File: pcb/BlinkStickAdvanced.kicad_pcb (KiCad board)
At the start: 2 copper layers, 37.1 x 59.3 mm, 31 parts, among them J1 POWER, J2 USB_B_Micro, J3 ADD_HEADER_B, J4 ADD_HEADER_G, J5 ADD_HEADER_R, J6 RGB_HEADER, J7 RGB_HEADER, Q1 IRLR8726, Q2 IRLR8726, Q3 IRLR8726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

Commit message: PCB Change Silkscreen
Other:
- board text added: "BlinkStick Advanced (c) Foxdogface & Agile Inovative Ltd github.com/Foxdogface/BlinkStickAdvanced"
- board text removed: "BlinkStick Advanced Foxdogface & Agile Inovative Ltd"
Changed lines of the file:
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@@
   (gr_poly
     (pts
-      (xy 49.852241 42.689652)
-      (xy 49.852241 43.138906)
-      (xy 45.093779 43.138906)
-      (xy 45.093779 44.037292)
-      (xy 49.852241 44.037292)
-      (xy 49.852241 44.48691)
-      (xy 55.64193 44.48691)
-      (xy 55.64193 42.689652)
-      (xy 49.852241 42.689652)
-    ) (layer "B.SilkS") (width 0.2) (fill solid))
+      (xy 55.181249 76.88263)
+      (xy 55.181249 76.972481)
+      (xy 54.229556 76.972481)
+      (xy 54.229556 77.152158)
+      (xy 55.181249 77.152158)
+      (xy 55.181249 77.242082)
+      (xy 56.339186 77.242082)
+      (xy 56.339186 76.88263)
+      (xy 55.181249 76.88263)
+    ) (layer "B.SilkS") (width 0.008) (fill solid))
   (gr_poly
     (pts
-      (xy 49.852241 49.926867)
-      (xy 49.852241 50.376667)
-      (xy 43.596186 50.376667)
-      (xy 43.596186 51.27487)
-      (xy 49.852241 51.27487)
-      (xy 49.852241 51.724306)
-      (xy 55.64193 51.724306)
-      (xy 55.64193 49.926867)
-      (xy 49.852241 49.926867)
-    ) (layer "B.SilkS") (width 0.2) (fill solid))
+      (xy 55.181249 78.330073)
+      (xy 55.181249 78.420033)
+      (xy 53.930038 78.420033)
+      (xy 53.930038 78.599674)
+      (xy 55.181249 78.599674)
+      (xy 55.181249 78.689561)
+      (xy 56.339186 78.689561)
+      (xy 56.339186 78.330073)
+      (xy 55.181249 78.330073)
+    ) (layer "B.SilkS") (width 0.008) (fill solid))
   (gr_poly
     (pts
-      (xy 61.13256 53.3883)
-      (xy 61.13256 41.142235)
-      (xy 64.593265 41.142235)
-      (xy 64.908331 41.150203)
-      (xy 65.21926 41.173849)
-      (xy 65.525669 41.212789)
-      (xy 65.827172 41.266638)
-      (xy 66.123385 41.335011)
-      (xy 66.413924 41.417524)
-      (xy 66.698403 41.513792)
-      (xy 66.976437 41.62343)
-      (xy 67.247643 41.746054)
-      (xy 67.511635 41.881279)
-      (xy 67.768029 42.02872)
-      (xy 68.01644 42.187992)
-      (xy 68.256483 42.358711)
-      (xy 68.487774 42.540491)
-      (xy 68.709928 42.732949)
-      (xy 68.922561 42.9357)
-      (xy 69.125286 43.148359)
-      (xy 69.317721 43.37054)
-      (xy 69.49948 43.60186)
-      (xy 69.670178 43.841934)
-      (xy 69.829432 44.090376)
-      (xy 69.976855 44.346803)
-      (xy 70.112064 44.61083)
-      (xy 70.234673 44.882071)
-      (xy 70.344299 45.160143)
-      (xy 70.440556 45.444659)
-      (xy 70.52306 45.735237)
-      (xy 70.591425 46.03149)
-      (xy 70.645268 46.333035)
-      (xy 70.684204 46.639487)
-      (xy 70.707847 46.95046)
-      (xy 70.715814 47.26557)
-      (xy 70.707846 47.580594)
-      (xy 70.6842 47.891488)
-      (xy 70.645259 48.197868)
-      (xy 70.59141 48.499348)
-      (xy 70.523037 48.795544)
-      (xy 70.440524 49.086071)
-      (xy 70.344257 49.370543)
-      (xy 70.234621 49.648575)
-      (xy 70.112 49.919783)
-      (xy 69.97678 50.183782)
-      (xy 69.829345 50.440185)
-      (xy 69.670079 50.688609)
-      (xy 69.499369 50.928668)
-      (xy 69.317599 51.159977)
-      (xy 69.125153 51.382151)
-      (xy 68.922417 51.594805)
-      (xy 68.709775 51.797554)
-      (xy 68.487613 51.990013)
-      (xy 68.256315 52.171798)
-      (xy 68.016266 52.342521)
-      (xy 67.767851 52.5018)
-      (xy 67.511455 52.649249)
-      (xy 67.247462 52.784482)
-      (xy 66.976258 52.907115)
-      (xy 66.698228 53.016762)
-      (xy 66.413757 53.11304)
-      (xy 66.123228 53.195561)
-      (xy 65.827028 53.263943)
-      (xy 65.52554 53.317798)
-      (xy 65.219151 53.356743)
-      (xy 64.908244 53.380393)
-      (xy 64.593205 53.388361)
-      (xy 61.13256 53.388361)
-      (xy 61.13256 53.3883)
-    ) (layer "B.SilkS") (width 0.2) (fill solid))
+      (xy 57.250936 76.320222)
+      (xy 56.532166 76.320222)
+      (xy 56.532166 79.381775)
+      (xy 57.250936 79.381775)
+      (xy 57.250936 76.320222)
+    ) (layer "B.SilkS") (width 0.008) (fill solid))
   (gr_poly
     (pts
-      (xy 60.200676 39.877612)
-      (xy 56.606829 39.877612)
-      (xy 56.606829 55.185377)
-      (xy 60.200677 55.185377)
-      (xy 60.200677 39.877612)
-      (xy 60.200676 39.877612)
-    ) (layer "B.SilkS") (width 0.2) (fill solid))
+      (xy 57.437312 79.02236)
+      (xy 57.437312 76.573147)
+      (xy 58.129453 76.573147)
+      (xy 58.192467 76.57474)
+      (xy 58.254652 76.579469)
+      (xy 58.315934 76.587257)
+      (xy 58.376235 76.598027)
+      (xy 58.435477 76.611702)
+      (xy 58.493585 76.628204)
+      (xy 58.550481 76.647458)
+      (xy 58.606088 76.669386)
+      (xy 58.660329 76.69391)
+      (xy 58.713127 76.720955)
+      (xy 58.764406 76.750444)
+      (xy 58.814088 76.782298)
+      (xy 58.862097 76.816442)
+      (xy 58.908355 76.852798)
+      (xy 58.952786 76.891289)
+      (xy 58.995313 76.93184)
+      (xy 59.035858 76.974371)
+      (xy 59.074345 77.018808)
+      (xy 59.110696 77.065072)
+      (xy 59.144836 77.113086)
+      (xy 59.176687 77.162775)
+      (xy 59.206171 77.21406)
+      (xy 59.233213 77.266866)
+      (xy 59.257735 77.321114)
+      (xy 59.27966 77.376728)
+      (xy 59.298912 77.433631)
+      (xy 59.315412 77.491747)
+      (xy 59.329085 77.550998)
+      (xy 59.339854 77.611307)
+      (xy 59.347641 77.672597)
+      (xy 59.35237 77.734792)
+      (xy 59.353963 77.797814)
+      (xy 59.35237 77.860818)
+      (xy 59.34764 77.922997)
+      (xy 59.339852 77.984273)
+      (xy 59.329082 78.044569)
+      (xy 59.315408 78.103808)
+      (xy 59.298905 78.161914)
+      (xy 59.279652 78.218808)
+      (xy 59.257725 78.274415)
+      (xy 59.2332 78.328656)
+      (xy 59.206156 78.381456)
+      (xy 59.176669 78.432737)
+      (xy 59.144816 78.482421)
+      (xy 59.110674 78.530433)
+      (xy 59.07432 78.576695)
+      (xy 59.035831 78.62113)
+      (xy 58.995284 78.663661)
+      (xy 58.952755 78.70421)
+      (xy 58.908323 78.742702)
+      (xy 58.862063 78.779059)
+      (xy 58.814054 78.813204)
+      (xy 58.764371 78.84506)
+      (xy 58.713091 78.874549)
+      (xy 58.660293 78.901596)
+      (xy 58.606052 78.926123)
+      (xy 58.550446 78.948052)
+      (xy 58.493552 78.967308)
+      (xy 58.435446 78.983812)
+      (xy 58.376206 78.997488)
+      (xy 58.315908 79.008259)
+      (xy 58.254631 79.016048)
+      (xy 58.192449 79.020778)
+      (xy 58.129441 79.022372)
+      (xy 57.437312 79.022372)
+      (xy 57.437312 79.02236)
+    ) (layer "B.SilkS") (width 0.008) (fill solid))
   (gr_line (start 70.618 57.604) (end 70.618 56.334) (layer "F.SilkS") (width 0.12))
   (gr_line (start 70.618 70.7485) (end 70.618 69.4785) (layer "F.SilkS") (width 0.12))
@@
   (gr_arc (start 41.154 93.435) (mid 39.357949 92.691051) (end 38.614 90.895) (layer "Edge.Cuts") (width 0.1))
   (gr_line (start 73.158 93.442349) (end 41.154 93.435) (layer "Edge.Cuts") (width 0.1))
-  (gr_text "BlinkStick Advanced\nFoxdogface & Agile Inovative Ltd" (at 46.736 68.326 270) (layer "B.SilkS")
-    (effects (font (size 1 1) (thickness 0.15)) (justify mirror))
+  (gr_text "BlinkStick Advanced\n(c) Foxdogface & Agile Inovative Ltd\ngithub.com/Foxdogface/BlinkStickAdvanced" (at 56.642 75.819 270) (layer "B.SilkS")
+    (effects (font (size 1 1) (thickness 0.15)) (justify left mirror))
   )
   (gr_text "+12" (at 69.602 69.4785 90) (layer "F.SilkS")
@@
     (effects (font (size 1 1) (thickness 0.15)))
   )
-  (gr_text "BlinkStick Advanced\nRev 1.0\n" (at 63.881 74.549 90) (layer "F.SilkS")
+  (gr_text "BlinkStick Advanced\nRev 1.0\n" (at 63.5 78.74 90) (layer "F.SilkS")
     (effects (font (size 1 1) (thickness 0.15)) (justify left))
   )
@@
     (effects (font (size 0.8 0.8) (thickness 0.12)))
   )
-  (gr_text "DI" (at 44.71 74.294 270) (layer "F.SilkS")
+  (gr_text "DI" (at 44.71 74.294) (layer "F.SilkS")
     (effects (font (size 1 1) (thickness 0.15)))
   )
@@
     )
   )
+  (group "" (id b1dad93c-ba77-40bd-9b75-65e2d6f9b5a1)
+    (members
+      4ccb0e93-36f7-4d7b-baba-2457a90267b7
+      5e182438-6e6f-45ba-bef5-6be708805673
+      5ed8deae-e8d8-451d-b355-245f684ec0f6
+      9fa8af66-62ad-41ac-afee-78344131d7e2
+    )
+  )
   (group "" (id dc577978-f61c-428e-9244-b42fcfc07f25)
     (members
@@
     )
   )
-  (group "" (id e15cedca-0c1c-4c6b-b473-17ab02d76cf9)
-    (members
-      057dff60-5b63-4365-8092-fe40ca4f6ba6
-      94f916ed-7d8d-4c18-a00c-ed22517e241d
-      f2962283-8d92-4dc3-8a08-f6b3cc18df8b
-      f6cc9d27-2a76-4bc5-bcfe-60cd92efc84c
-    )
-  )

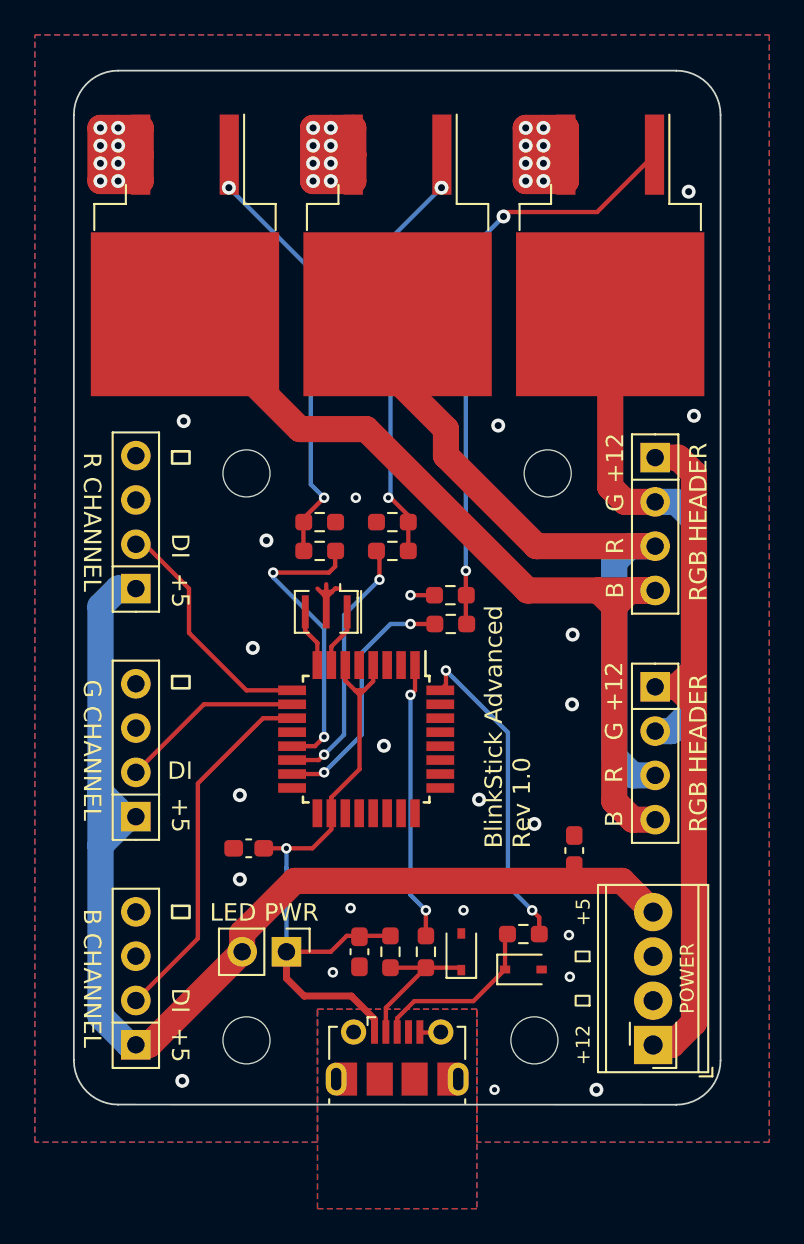
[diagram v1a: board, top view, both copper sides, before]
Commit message: PCB Change Silkscreen
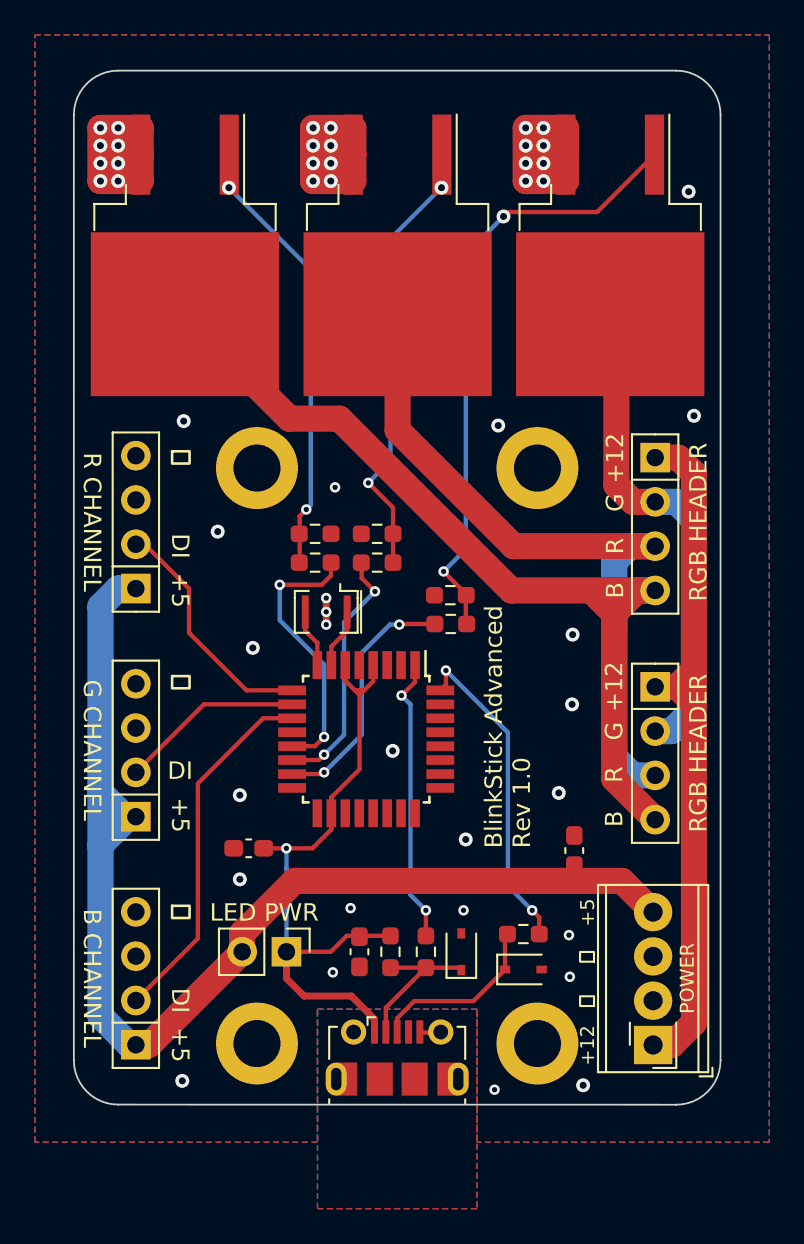
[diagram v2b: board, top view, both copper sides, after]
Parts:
- removed the REF** at (65.8, 57.2)
- removed the REF** at (65.0, 89.8)
- removed the REF** at (48.5, 57.2)
- removed the REF** at (48.5, 89.8)
- added REF**: MountingHole_2.7mm_M2.5_DIN965_Pad, MountingHole:MountingHole_2.7mm_M2.5_DIN965_Pad, F.Cu at (65.2, 89.9)
- added REF**: MountingHole_2.7mm_M2.5_DIN965_Pad, MountingHole:MountingHole_2.7mm_M2.5_DIN965_Pad, F.Cu at (49.1, 89.9)
- added REF**: MountingHole_2.7mm_M2.5_DIN965_Pad, MountingHole:MountingHole_2.7mm_M2.5_DIN965_Pad, F.Cu at (49.1, 56.9)
- added REF**: MountingHole_2.7mm_M2.5_DIN965_Pad, MountingHole:MountingHole_2.7mm_M2.5_DIN965_Pad, F.Cu at (65.2, 56.9)
- added REF**: KiCad-Logo2_5mm_SilkScreen, Symbol:KiCad-Logo2_5mm_SilkScreen, B.Cu at (45.2, 43.3)
- moved R8 1.10 mm to (56.0, 60.7)
- moved R5 1.10 mm to (56.0, 62.4)
- moved R7 0.72 mm to (52.5, 60.7)
- moved R4 0.72 mm to (52.5, 62.4)
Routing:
- net GND: track 46.2 -> 39.4 mm, vias 47 -> 49
- net /B_PWM: track 17.0 -> 15.7 mm
- net Net-(Q3-Pad1): track 34.4 -> 35.5 mm
- net Net-(Q2-Pad1): track 22.9 -> 23.8 mm
- net /B_OUT: track 51.5 -> 52.3 mm
- net /R_OUT: track 40.1 -> 40.9 mm

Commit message: USBaspLoader support for PCB.
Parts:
- added JP1: RST, TestPoint:TestPoint_2Pads_Pitch2.54mm_Drill0.8mm, F.Cu at (67.1, 68.6)
- added JP2: FLASH, Jumper:SolderJumper-2_P1.3mm_Open_TrianglePad1.0x1.5mm, F.Cu at (66.5, 66.3)
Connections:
- U1 pad 2: unconnected-(U1-Pad2) -> Net-(U1-Pad2)
- U1 pad 29: unconnected-(U1-Pad29) -> Net-(U1-Pad29)
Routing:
- net Net-(U1-Pad2): track 0.00 -> 9.53 mm
- net Net-(U1-Pad29): track 0.00 -> 7.83 mm
- net GND: vias 49 -> 54
